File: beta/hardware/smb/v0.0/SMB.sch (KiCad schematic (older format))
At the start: 24 parts, among them IC101 ATMEGA1284-A, J102 RTS_RESET, J103 ICSP, J104 SERIAL_REV, P101 I2C_CONN, P102 CONN_6, P103 CONN_5X2, P104 CONN_5X2, SW101 reset_sw, X101 16MHz

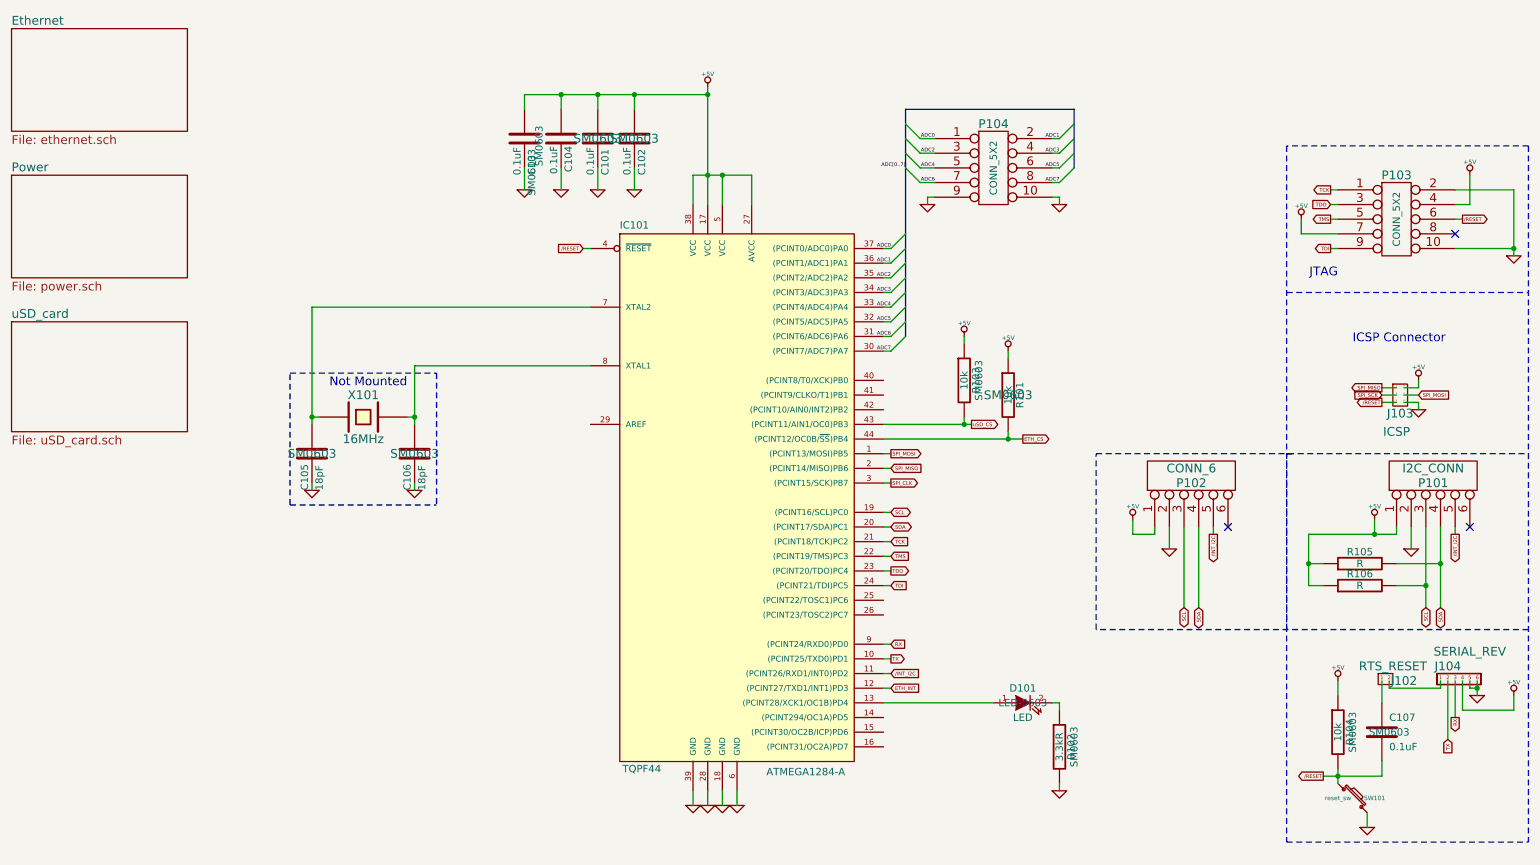
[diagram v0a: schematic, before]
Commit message: Layout and routing done, silkscreen done. Need review, and gerber check.
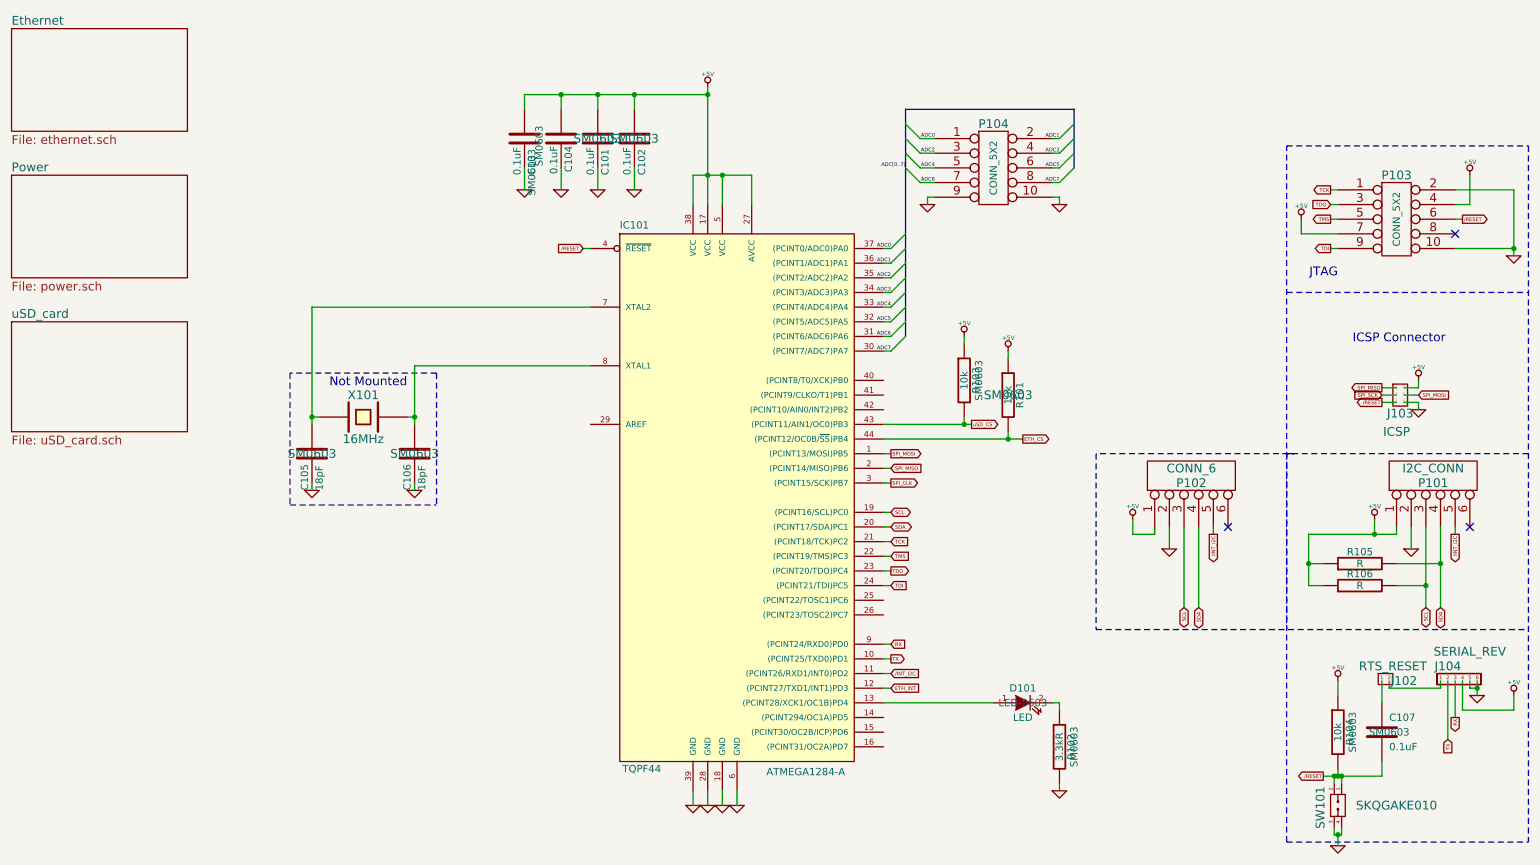
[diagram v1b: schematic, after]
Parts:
- removed SW101: reset_sw, symbol SW_PUSH_SMALL
- added SW101: SKQGAKE010, symbol SKQGAKE010
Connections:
- net /RESET: now also SW101.1, SW101.2
- net GND: now also SW101.3, SW101.4
